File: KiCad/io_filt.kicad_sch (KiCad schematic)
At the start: 60 parts, among them U27 SN74HCS08, U28 SN74LVC74AQPW, U29 SN74LVC74AQPW, U30 74HCT08PW, U31 ITS4200S-ME-P, U32 ITS4200S-ME-P, U33 ITS4200S-ME-P

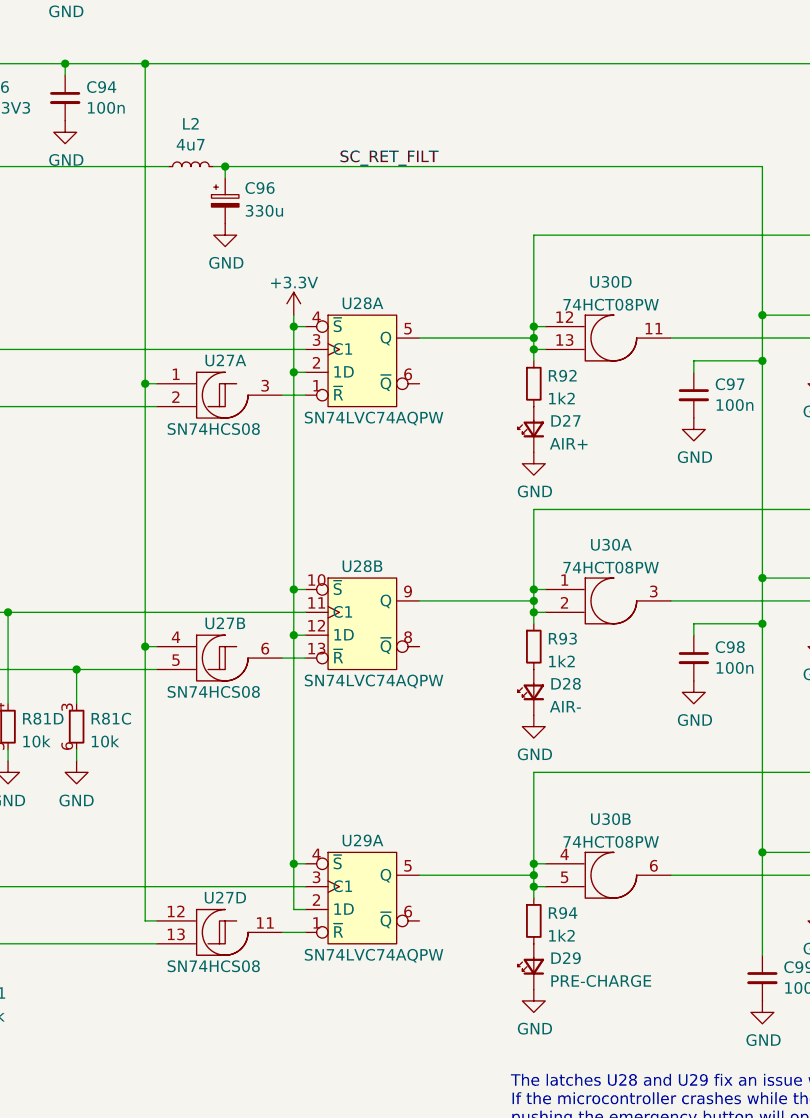
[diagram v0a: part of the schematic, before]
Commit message: Port to Kicad 7, small changes in auto-reset feature
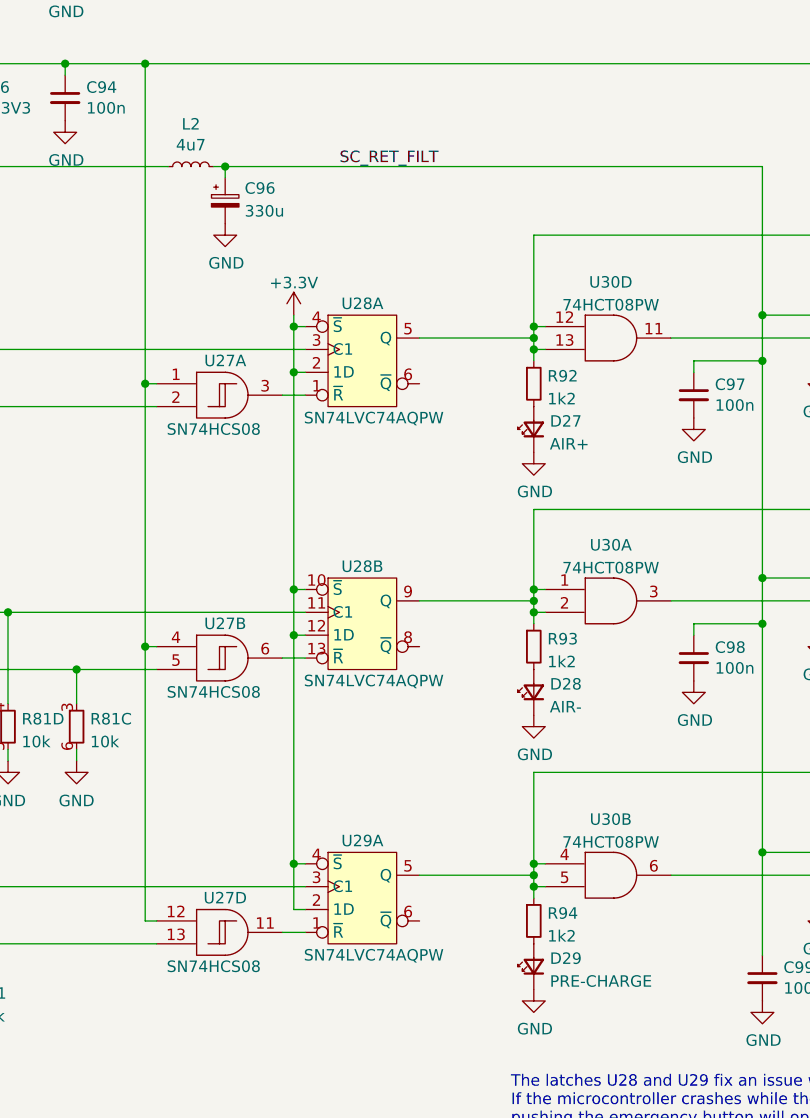
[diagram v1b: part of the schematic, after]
